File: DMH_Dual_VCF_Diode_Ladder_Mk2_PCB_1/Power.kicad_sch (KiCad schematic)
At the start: 38 parts, among them J0 Conn_01x01, J100 IDC_02x08, J23 Conn_01x04_PinHeader, U1 TL074, U10 TL074, U2 TL074, U3 TL074, U4 TL074, U5 TL074, U6 TL074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

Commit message: Corrected pin header footprint assignments
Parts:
- J23: footprint Connector_PinHeader_2.54mm:PinHeader_1x10_P2.54mm_Vertical -> Connector_PinHeader_2.54mm:PinHeader_1x04_P2.54mm_Vertical
- U10, U5, U6, U7, U8, U9: footprint (none) -> Package_DIP:DIP-14_W7.62mm_Socket
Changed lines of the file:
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@@
 			)
 		)
-		(property "Footprint" ""
+		(property "Footprint" "Package_DIP:DIP-14_W7.62mm_Socket"
 			(at 271.78 118.11 0)
 			(effects
@@
 			)
 		)
-		(property "Footprint" ""
+		(property "Footprint" "Package_DIP:DIP-14_W7.62mm_Socket"
 			(at 151.13 48.26 0)
 			(effects
@@
 			)
 		)
-		(property "Footprint" ""
+		(property "Footprint" "Package_DIP:DIP-14_W7.62mm_Socket"
 			(at 189.23 73.66 0)
 			(effects
@@
 			)
 		)
-		(property "Footprint" "Connector_PinHeader_2.54mm:PinHeader_1x10_P2.54mm_Vertical"
+		(property "Footprint" "Connector_PinHeader_2.54mm:PinHeader_1x04_P2.54mm_Vertical"
 			(at 88.9 57.15 0)
 			(effects
@@
 			)
 		)
-		(property "Footprint" ""
+		(property "Footprint" "Package_DIP:DIP-14_W7.62mm_Socket"
 			(at 248.92 118.11 0)
 			(effects
@@
 			)
 		)
-		(property "Footprint" ""
+		(property "Footprint" "Package_DIP:DIP-14_W7.62mm_Socket"
 			(at 189.23 48.26 0)
 			(effects
@@
 			)
 		)
-		(property "Footprint" "Connector_PinHeader_2.54mm:PinHeader_1x10_P2.54mm_Vertical"
+		(property "Footprint" "Connector_PinHeader_2.54mm:PinHeader_1x04_P2.54mm_Vertical"
 			(at 88.9 69.85 0)
 			(effects
@@
 			)
 		)
-		(property "Footprint" "Connector_PinHeader_2.54mm:PinHeader_1x10_P2.54mm_Vertical"
+		(property "Footprint" "Connector_PinHeader_2.54mm:PinHeader_1x04_P2.54mm_Vertical"
 			(at 88.9 50.8 0)
 			(effects
@@
 			)
 		)
-		(property "Footprint" ""
+		(property "Footprint" "Package_DIP:DIP-14_W7.62mm_Socket"
 			(at 151.13 73.66 0)
 			(effects
@@
 			)
 		)
-		(property "Footprint" ""
+		(property "Footprint" "Package_DIP:DIP-14_W7.62mm_Socket"
 			(at 227.33 73.66 0)
 			(effects
@@
 			)
 		)
-		(property "Footprint" ""
+		(property "Footprint" "Package_DIP:DIP-14_W7.62mm_Socket"
 			(at 223.52 118.11 0)
 			(effects
@@
 			)
 		)
-		(property "Footprint" ""
+		(property "Footprint" "Package_DIP:DIP-14_W7.62mm_Socket"
 			(at 227.33 48.26 0)
 			(effects
@@
 			)
 		)
-		(property "Footprint" "Connector_PinHeader_2.54mm:PinHeader_1x10_P2.54mm_Vertical"
+		(property "Footprint" "Connector_PinHeader_2.54mm:PinHeader_1x04_P2.54mm_Vertical"
 			(at 88.9 63.5 0)
 			(effects

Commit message: Adding buffered input to CV3 - in progress
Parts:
- removed unit 2 of U7
- removed unit 3 of U8

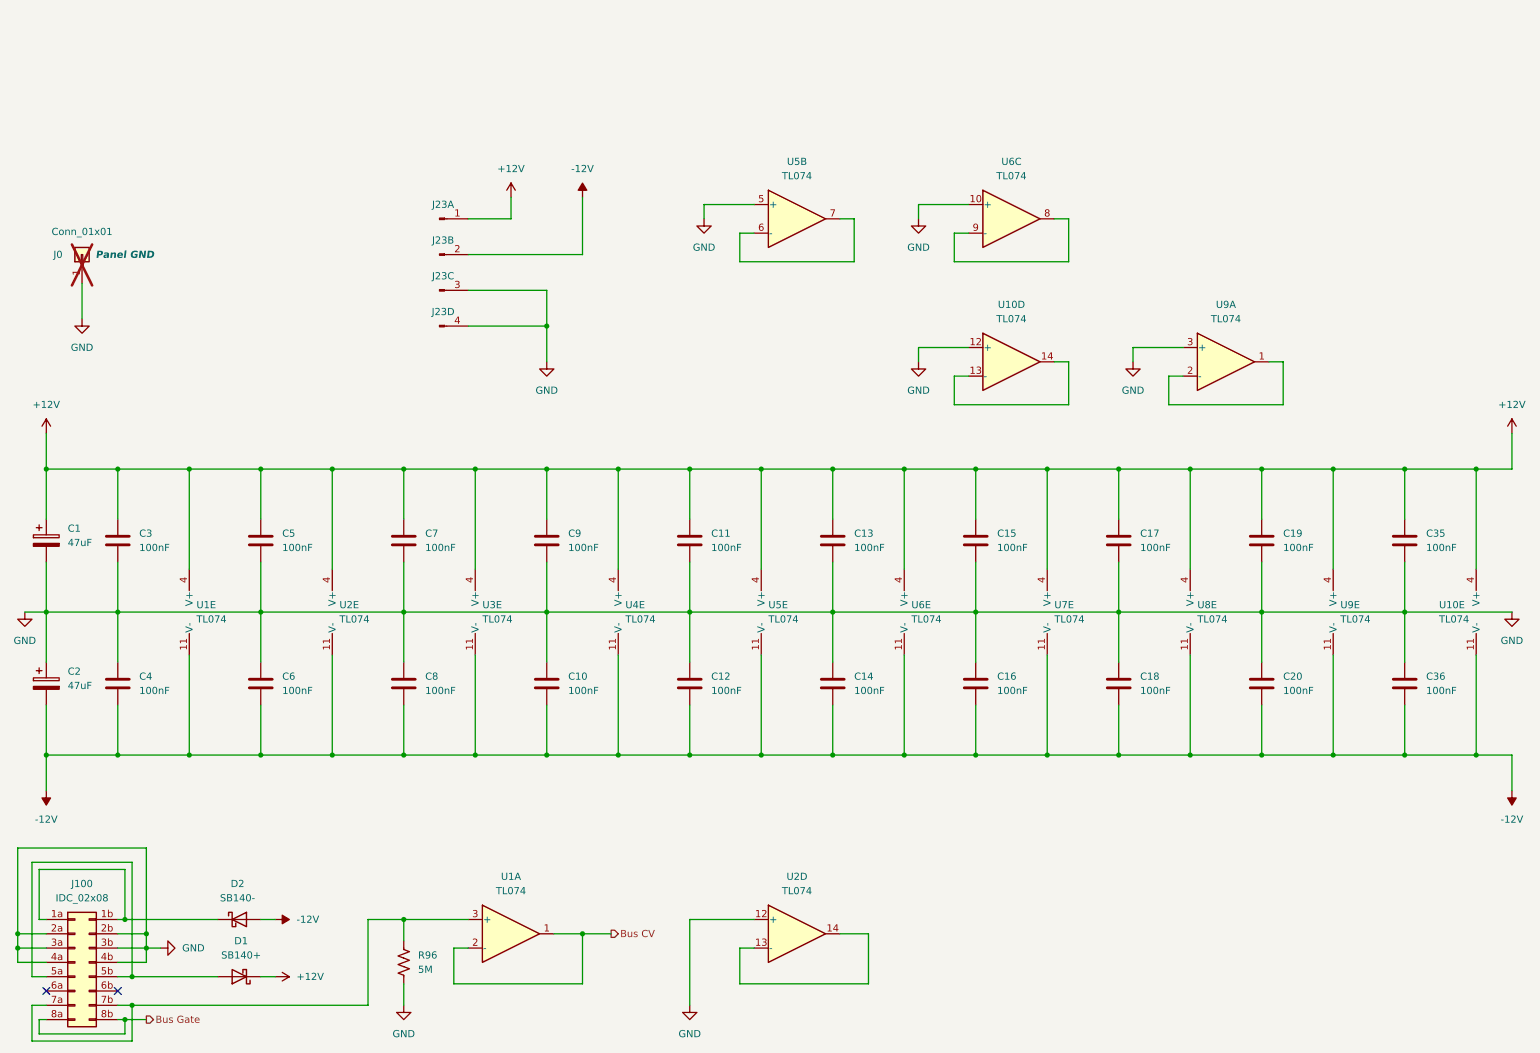
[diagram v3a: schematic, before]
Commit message: Added buffering to each CV 3 input separately
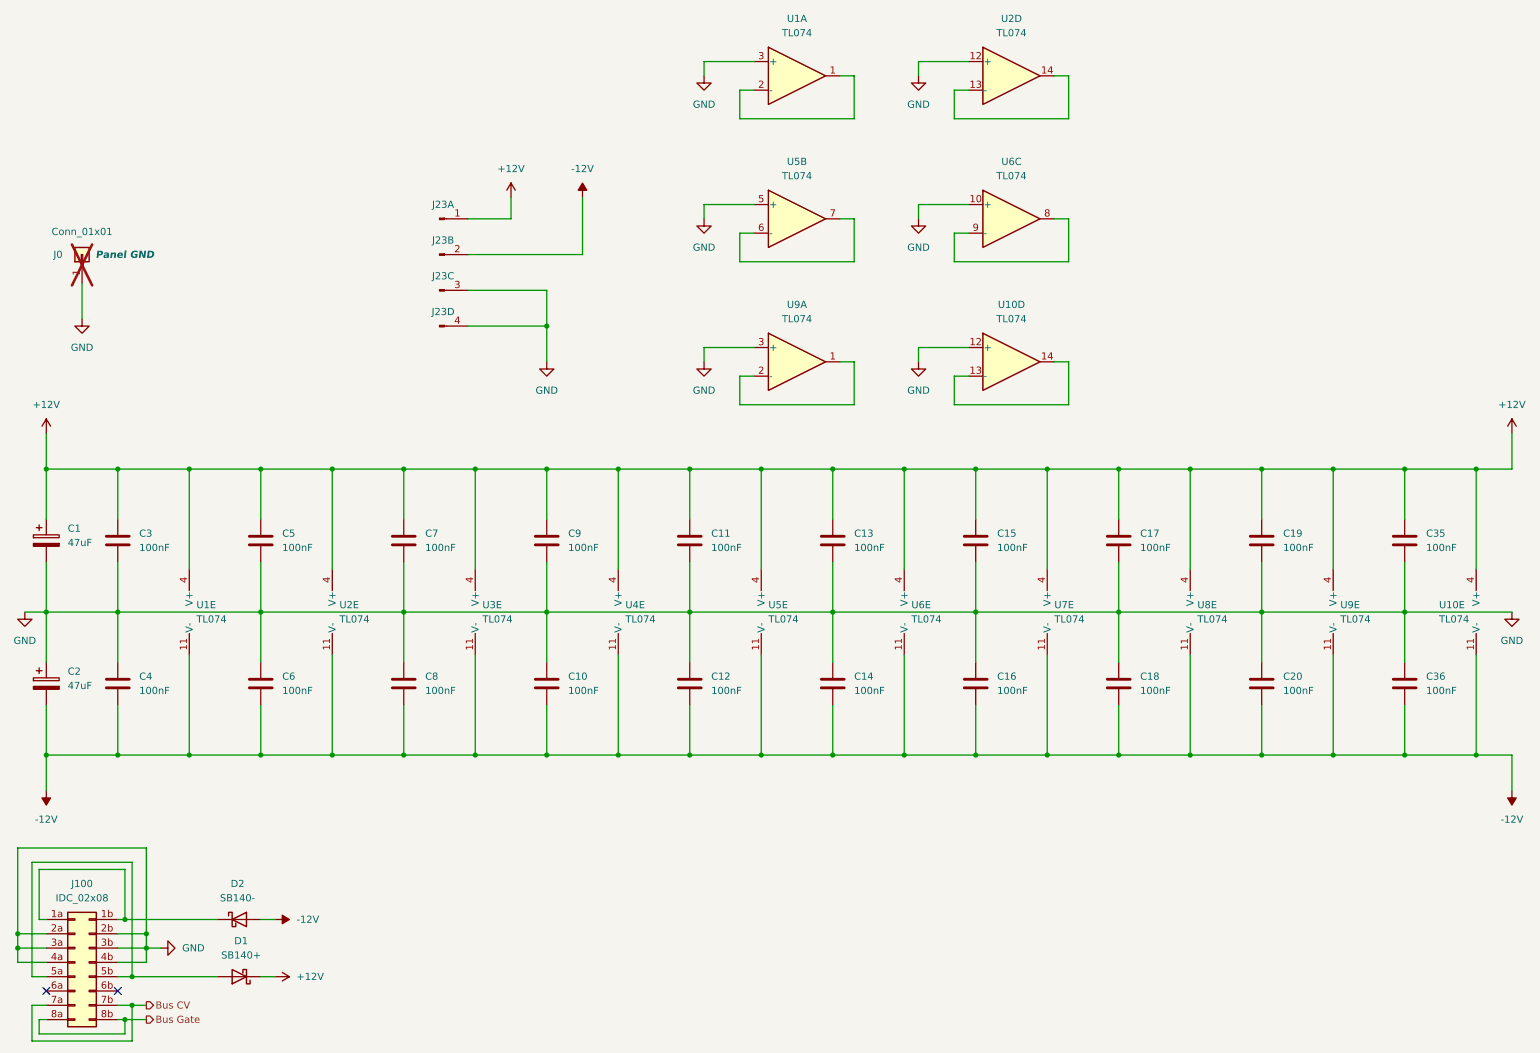
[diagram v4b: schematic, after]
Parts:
- removed R96: 5M, Resistor_THT:R_Axial_DIN0207_L6.3mm_D2.5mm_P7.62mm_Horizontal, symbol Device:R_US
- U1: footprint Package_DIP:DIP-14_W7.62mm_Socket -> (none)
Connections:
- net Bus CV: now also J100.7a (Pin_7a), J100.7b (Pin_7b); no longer U1.1, U1.2 (-)
- net GND: now also U1.3 (+)
- new net: U1.1, U1.2 (-)
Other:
- moved on the sheet: U2D, U9A

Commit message: Finished Mk2.0
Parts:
- U1: footprint (none) -> Package_DIP:DIP-14_W7.62mm_Socket
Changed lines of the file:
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@@
 			)
 		)
-		(property "Footprint" ""
+		(property "Footprint" "Package_DIP:DIP-14_W7.62mm_Socket"
 			(at 151.13 22.86 0)
 			(effects

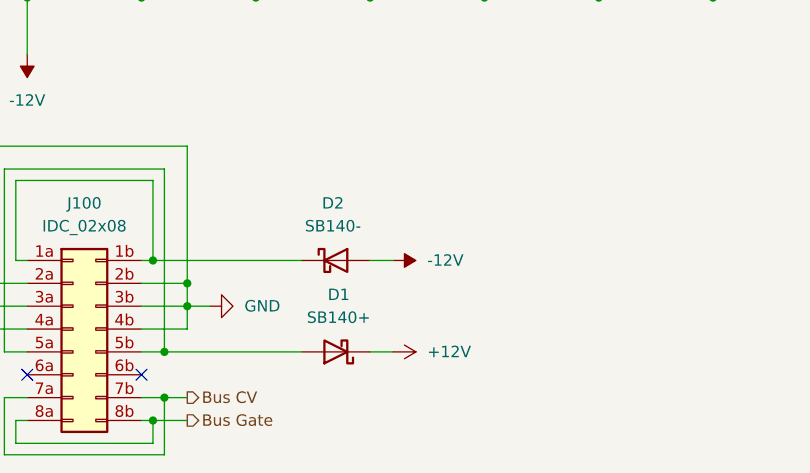
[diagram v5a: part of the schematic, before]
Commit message: KiCad 9.0.7 + centralized library
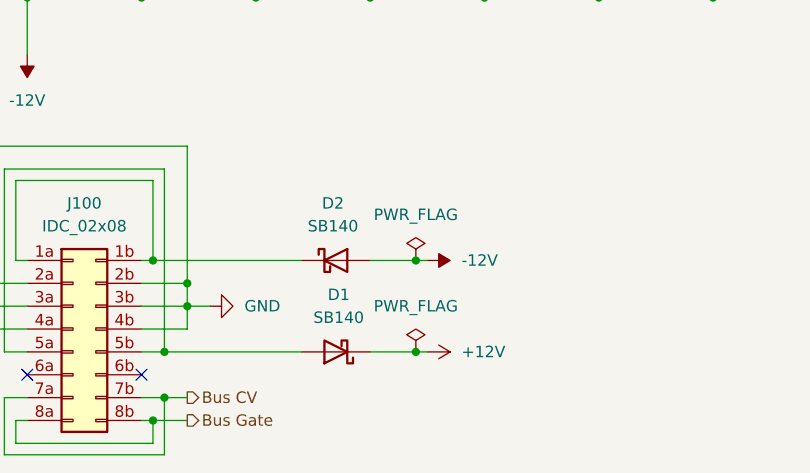
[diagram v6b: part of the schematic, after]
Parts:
- D1: value SB140+ -> SB140; symbol SynthStuff:Power_Bus_Schotty_+ -> Diode:SB140
- D2: value SB140- -> SB140; symbol SynthStuff:Power_Bus_Schotty_- -> Diode:SB140
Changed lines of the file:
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@@
 	)
 	(junction
+		(at 62.23 185.42)
+		(diameter 0)
+		(color 0 0 0 0)
+	)
+	(junction
 		(at 57.15 146.05)
 		(diameter 0)
@@
 	)
 	(junction
+		(at 62.23 175.26)
+		(diameter 0)
+		(color 0 0 0 0)
+	)
+	(junction
 		(at 69.85 146.05)
 		(diameter 0)
@@
 	(wire
 		(pts
+			(xy 62.23 185.42) (xy 63.5 185.42)
+		)
+		(stroke
+			(width 0)
+			(type default)
+		)
+	)
+	(wire
+		(pts
 			(xy 69.85 146.05) (xy 82.55 146.05)
 		)
@@
 	(wire
 		(pts
+			(xy 57.15 185.42) (xy 62.23 185.42)
+		)
+		(stroke
+			(width 0)
+			(type default)
+		)
+	)
+	(wire
+		(pts
 			(xy 162.56 25.4) (xy 160.02 25.4)
 		)
@@
 	(wire
 		(pts
-			(xy 57.15 175.26) (xy 59.69 175.26)
-		)
-		(stroke
-			(width 0)
-			(type default)
-		)
-	)
-	(wire
-		(pts
 			(xy 200.66 50.8) (xy 198.12 50.8)
 		)
@@
 	(wire
 		(pts
-			(xy 57.15 185.42) (xy 59.69 185.42)
-		)
-		(stroke
-			(width 0)
-			(type default)
-		)
-	)
-	(wire
-		(pts
 			(xy 142.24 58.42) (xy 162.56 58.42)
 		)
@@
 	(wire
 		(pts
+			(xy 57.15 175.26) (xy 62.23 175.26)
+		)
+		(stroke
+			(width 0)
+			(type default)
+		)
+	)
+	(wire
+		(pts
 			(xy 57.15 95.25) (xy 69.85 95.25)
 		)
@@
 	(wire
 		(pts
+			(xy 62.23 175.26) (xy 63.5 175.26)
+		)
+		(stroke
+			(width 0)
+			(type default)
+		)
+	)
+	(wire
+		(pts
 			(xy 135.89 50.8) (xy 135.89 48.26)
 		)
@@
 	(symbol
 		(lib_id "power:+12V")
-		(at 59.69 185.42 270)
+		(at 63.5 185.42 270)
 		(unit 1)
 		(exclude_from_sim no)
@@
 		(fields_autoplaced yes)
 		(property "Reference" "#PWR02"
-			(at 55.88 185.42 0)
+			(at 59.69 185.42 0)
 			(effects
 				(font
@@
 		)
 		(property "Value" "+12V"
-			(at 63.5 185.4199 90)
+			(at 67.31 185.4199 90)
 			(effects
 				(font
@@
 		)
 		(property "Footprint" ""
-			(at 59.69 185.42 0)
+			(at 63.5 185.42 0)
 			(effects
 				(font
@@
 		)
 		(property "Datasheet" ""
-			(at 59.69 185.42 0)
+			(at 63.5 185.42 0)
 			(effects
 				(font
@@
 		)
 		(property "Description" "Power symbol creates a global label with name \"+12V\""
-			(at 59.69 185.42 0)
+			(at 63.5 185.42 0)
 			(effects
 				(font
@@
 	)
 	(symbol
+		(lib_id "power:PWR_FLAG")
+		(at 62.23 175.26 0)
+		(unit 1)
+		(exclude_from_sim no)
+		(in_bom yes)
+		(on_board yes)
+		(dnp no)
+		(fields_autoplaced yes)
+		(property "Reference" "#FLG01"
+			(at 62.23 173.355 0)
+			(effects
+				(font
+					(size 1.27 1.27)
+				)
+				(hide yes)
+			)
+		)
+		(property "Value" "PWR_FLAG"
+			(at 62.23 170.18 0)
+			(effects
+				(font
+					(size 1.27 1.27)
+				)
+			)
+		)
+		(property "Footprint" ""
+			(at 62.23 175.26 0)
+			(effects
+				(font
+					(size 1.27 1.27)
+				)
+				(hide yes)
+			)
+		)
+		(property "Datasheet" "~"
+			(at 62.23 175.26 0)
+			(effects
+				(font
+					(size 1.27 1.27)
+				)
+				(hide yes)
+			)
+		)
+		(property "Description" "Special symbol for telling ERC where power comes from"
+			(at 62.23 175.26 0)
+			(effects
+				(font
+					(size 1.27 1.27)
+				)
+				(hide yes)
+			)
+		)
+		(pin "1"
+		)
+		(instances
+			(project ""
+				(path "/58f4306d-5387-4983-bb08-41a2313fd315/0cdf34b2-39cd-4d9e-981a-97cd34791509"
+					(reference "#FLG01")
+					(unit 1)
+				)
+			)
+		)
+	)
+	(symbol
 		(lib_id "power:GND")
 		(at 39.37 180.34 90)
@@
 	)
 	(symbol
+		(lib_id "power:PWR_FLAG")
+		(at 62.23 185.42 0)
+		(unit 1)
+		(exclude_from_sim no)
+		(in_bom yes)
+		(on_board yes)
+		(dnp no)
+		(fields_autoplaced yes)
+		(property "Reference" "#FLG02"
+			(at 62.23 183.515 0)
+			(effects
+				(font
+					(size 1.27 1.27)
+				)
+				(hide yes)
+			)
+		)
+		(property "Value" "PWR_FLAG"
+			(at 62.23 180.34 0)
+			(effects
+				(font
+					(size 1.27 1.27)
+				)
+			)
+		)
+		(property "Footprint" ""
+			(at 62.23 185.42 0)
+			(effects
+				(font
+					(size 1.27 1.27)
+				)
+				(hide yes)
+			)
+		)
+		(property "Datasheet" "~"
+			(at 62.23 185.42 0)
+			(effects
+				(font
+					(size 1.27 1.27)
+				)
+				(hide yes)
+			)
+		)
+		(property "Description" "Special symbol for telling ERC where power comes from"
+			(at 62.23 185.42 0)
+			(effects
+				(font
+					(size 1.27 1.27)
+				)
+				(hide yes)
+			)
+		)
+		(pin "1"
+		)
+		(instances
+			(project ""
+				(path "/58f4306d-5387-4983-bb08-41a2313fd315/0cdf34b2-39cd-4d9e-981a-97cd34791509"
+					(reference "#FLG02")
+					(unit 1)
+				)
+			)
+		)
+	)
+	(symbol
 		(lib_id "Amplifier_Operational:TL074")
 		(at 190.5 50.8 0)
@@
 	(symbol
 		(lib_id "power:-12V")
-		(at 59.69 175.26 270)
+		(at 63.5 175.26 270)
 		(unit 1)
 		(exclude_from_sim no)
@@
 		(fields_autoplaced yes)
 		(property "Reference" "#PWR01"
-			(at 55.88 175.26 0)
+			(at 59.69 175.26 0)
 			(effects
 				(font
@@
 		)
 		(property "Value" "-12V"
-			(at 63.5 175.2599 90)
+			(at 67.31 175.2599 90)
 			(effects
 				(font
@@
 		)
 		(property "Footprint" ""
-			(at 59.69 175.26 0)
+			(at 63.5 175.26 0)
 			(effects
 				(font
@@
 		)
 		(property "Datasheet" ""
-			(at 59.69 175.26 0)
+			(at 63.5 175.26 0)
 			(effects
 				(font
@@
 		)
 		(property "Description" "Power symbol creates a global label with name \"-12V\""
-			(at 59.69 175.26 0)
+			(at 63.5 175.26 0)
 			(effects
 				(font
@@
 	)
 	(symbol
-		(lib_id "SynthStuff:Power_Bus_Schotty_-")
+		(lib_id "Diode:SB140")
 		(at 53.34 175.26 0)
 		(unit 1)
@@
 			)
 		)
-		(property "Value" "SB140-"
+		(property "Value" "SB140"
 			(at 53.0225 171.45 0)
 			(effects
@@
 	)
 	(symbol
-		(lib_id "SynthStuff:Power_Bus_Schotty_+")
+		(lib_id "Diode:SB140")
 		(at 53.34 185.42 180)
 		(unit 1)
@@
 			)
 		)
-		(property "Value" "SB140+"
+		(property "Value" "SB140"
 			(at 53.6575 181.61 0)
 			(effects
